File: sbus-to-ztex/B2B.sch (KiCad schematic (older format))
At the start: 8 parts, among them J1 Conn_01x06_Male, J3 Conn_02x07_Odd_Even

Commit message: Commit first go at v1.2
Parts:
- removed DOE2: RED, LED_SMD:LED_0805_2012Metric, symbol Device:LED_ALT
- removed ROE2: 549, Resistor_SMD:R_0603_1608Metric, symbol Device:R
- J1: footprint Connector_PinHeader_2.54mm:PinHeader_1x06_P2.54mm_Vertical -> Connector_PinHeader_2.54mm:PinHeader_1x06_P2.54mm_Horizontal; MPN 22-28-4060 -> 22-28-8060; MPN-ALT (none) -> PZ254R-11-06P; URL (none) -> https://www2.mouser.com/ProductDetail/Molex/22-28-8060?qs=4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
- J3: MPN 878331420 -> 87833-1420; MPN-ALT (none) -> A2005WR-N-2X7P-B; URL (none) -> https://www2.mouser.com/ProductDetail/Molex/87833-1420?qs=%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
- JAB1, JCD1: URL (none) -> https://www2.mouser.com/ProductDetail/Molex/10-89-7642?qs=%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
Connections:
- net SBUS_3V3_INT[4]*: now also JCD1.40 (N5~IO_L13P_T2_MRCC_34)
- net SBUS_3V3_INT[7]*: no longer JCD1.40 (N5~IO_L13P_T2_MRCC_34)
- net PMOD-8: now reaches JCD1.20 (U4~IO_L8P_T1_34)
- net LED0 renamed USBH0_D+
- net LED1 renamed USBH0_D-
- net LED2 renamed PMOD-12
- net LED3 renamed PMOD-11
- net LED4 renamed PMOD-10
- net LED5 renamed PMOD-9
- net LED6 renamed PMOD-7
- net LED7 renamed PMOD-5
- net SBUS_DATA_OE_LED_2 renamed PMOD-6
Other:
- note removed: "Free"
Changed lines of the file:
@@
 $Descr A4 11693 8268
 encoding utf-8
-Sheet 3 5
+Sheet 3 6
 Title "sbus-to-ztex B2B connector"
 Date ""
@@
 F 3 "" H 1800 2650 50  0001 C CNN
 F 4 "10-89-7642" H 1800 2650 50  0001 C CNN "MPN"
+F 5 "https://www2.mouser.com/ProductDetail/Molex/10-89-7642?qs=%2Fha2pyFadugCxzQFZUdvioDcljDVidgd4vXrOFuSRYM%3D" H 1800 2650 50  0001 C CNN "URL"
 	1    1800 2650
 	1    0    0    -1
@@
 Text GLabel 4100 2850 2    60   Input ~ 0
 SBUS_3V3_D[24]
-Text GLabel 9900 3050 2    60   Input ~ 0
+Text GLabel 6650 5700 2    60   Input ~ 0
 SBUS_3V3_INT[7]*
 Text GLabel 6300 5850 0    60   Input ~ 0
@@
 Text GLabel 6300 5950 0    60   Input ~ 0
 SBUS_3V3_INT[5]*
-Text GLabel 6300 6050 0    60   Input ~ 0
+Text GLabel 9900 3050 2    60   Input ~ 0
 SBUS_3V3_INT[4]*
 Text GLabel 6300 6150 0    60   Input ~ 0
@@
 Text GLabel 7400 2350 0    60   Input ~ 0
 SBUS_3V3_EER*
-Text GLabel 7400 1450 0    60   Input ~ 0
-LED0
-Text GLabel 7400 1550 0    60   Input ~ 0
-LED1
 Wire Wire Line
 	1800 5850 1650 5850
@@
 F 0 "J1" H 9356 1228 50  0000 C CNN
 F 1 "Conn_01x06_Male" H 9356 1137 50  0000 C CNN
-F 2 "Connector_PinHeader_2.54mm:PinHeader_1x06_P2.54mm_Vertical" H 9250 850 50  0001 C CNN
+F 2 "Connector_PinHeader_2.54mm:PinHeader_1x06_P2.54mm_Horizontal" H 9250 850 50  0001 C CNN
 F 3 "~" H 9250 850 50  0001 C CNN
-F 4 "22-28-4060" H 9250 850 50  0001 C CNN "MPN"
+F 4 "22-28-8060" H 9250 850 50  0001 C CNN "MPN"
+F 5 "PZ254R-11-06P" H 9250 850 50  0001 C CNN "MPN-ALT"
+F 6 "https://www2.mouser.com/ProductDetail/Molex/22-28-8060?qs=4XSMV6Twtb2rYD%2F%2F316gfQ==" H 9250 850 50  0001 C CNN "URL"
 	1    9250 850
 	1    0    0    -1
@@
 F 3 "" H 7600 2650 50  0001 C CNN
 F 4 "10-89-7642" H 7600 2650 50  0001 C CNN "MPN"
+F 5 "https://www2.mouser.com/ProductDetail/Molex/10-89-7642?qs=%2Fha2pyFadugCxzQFZUdvioDcljDVidgd4vXrOFuSRYM%3D" H 7600 2650 50  0001 C CNN "URL"
 	1    7600 2650
 	1    0    0    -1
 $EndComp
-Text GLabel 7400 1650 0    60   Input ~ 0
-LED2
-Text GLabel 7400 1750 0    60   Input ~ 0
-LED3
 Text GLabel 2800 5850 2    60   Input ~ 12
 SBUS_DATA_OE_LED
@@
 Text GLabel 9900 2350 2    60   Input ~ 12
 SBUS_DATA_OE_LED
-Wire Wire Line
-	1800 6400 1650 6400
-Wire Wire Line
-	1650 6400 1650 6600
-Wire Wire Line
-	2100 6400 2500 6400
-$Comp
-L Device:R ROE?
-U 1 1 5F75534A
-P 2650 6400
-AR Path="/5F6B165A/5F75534A" Ref="ROE?"  Part="1"
-AR Path="/5F67E4B9/5F75534A" Ref="ROE2"  Part="1"
-F 0 "ROE2" V 2730 6400 50  0000 C CNN
-F 1 "549" V 2650 6400 50  0000 C CNN
-F 2 "Resistor_SMD:R_0603_1608Metric" V 2580 6400 50  0001 C CNN
-F 3 "" H 2650 6400 50  0000 C CNN
-F 4 "0603WAF5490T5E" V 2650 6400 50  0001 C CNN "MPN"
-	1    2650 6400
-	0    1    1    0
-$EndComp
-Text Label 2150 6400 0    60   ~ 0
-DATA_OE_LED_2
-$Comp
-L Device:LED_ALT D?
-U 1 1 5F75535B
-P 1950 6400
-AR Path="/5F6B165A/5F75535B" Ref="D?"  Part="1"
-AR Path="/5F67E4B9/5F75535B" Ref="DOE2"  Part="1"
-F 0 "DOE2" H 1950 6500 50  0000 C CNN
-F 1 "RED" H 1600 6400 50  0000 R CNN
-F 2 "LED_SMD:LED_0805_2012Metric" H 1950 6400 50  0001 C CNN
-F 3 "https://optoelectronics.liteon.com/upload/download/DS-22-99-0150/LTST-C170KRKT.pdf" H 1950 6400 50  0001 C CNN
-F 4 "www.liteon.com" H 1950 6400 60  0001 C CNN "MNF1_URL"
-F 5 "LTST-C170KRKT" H 1950 6400 60  0001 C CNN "MPN"
-F 6 "859-LTST-C170KRKT" H 1950 6400 60  0001 C CNN "Mouser"
-F 7 "743-IN-S85ATR" H 1950 6400 50  0001 C CNN "Mouse_r2"
-F 8 "160-1415-1-ND" H 1950 6400 50  0001 C CNN "Digikey"
-F 9 "C94868" H 1950 6400 50  0001 C CNN "LCSC"
-F 10 "0.0195$" H 1950 6400 50  0001 C CNN "price400_LCSC"
-F 11 "FV007" H 1950 6400 50  0001 C CNN "Koncar"
-F 12 "TB" H 1950 6400 50  0001 C CNN "Side"
-	1    1950 6400
-	1    0    0    -1
-$EndComp
-$Comp
-L power:GND #PWR0120
-U 1 1 5F755362
-P 1650 6600
-F 0 "#PWR0120" H 1650 6350 50  0001 C CNN
-F 1 "GND" H 1655 6427 50  0000 C CNN
-F 2 "" H 1650 6600 50  0001 C CNN
-F 3 "" H 1650 6600 50  0001 C CNN
-	1    1650 6600
-	1    0    0    -1
-$EndComp
-Text GLabel 2800 6400 2    60   Input ~ 12
-SBUS_DATA_OE_LED_2
-Text GLabel 9900 2450 2    60   Input ~ 12
-SBUS_DATA_OE_LED_2
 $Comp
 L Connector_Generic:Conn_02x07_Odd_Even J3
@@
 F 2 "Connector_PinHeader_2.00mm:PinHeader_2x07_P2.00mm_Horizontal" H 3150 7250 50  0001 C CNN
 F 3 "https://www.molex.com/pdm_docs/sd/878331420_sd.pdf" H 3150 7250 50  0001 C CNN
-F 4 "878331420" H 3150 7250 50  0001 C CNN "MPN"
+F 4 "87833-1420" H 3150 7250 50  0001 C CNN "MPN"
+F 5 "A2005WR-N-2X7P-B" H 3150 7250 50  0001 C CNN "MPN-ALT"
+F 6 "https://www2.mouser.com/ProductDetail/Molex/87833-1420?qs=%2Fha2pyFadujYFYCIYI1IvFCvLi7no9WQYzIL%2FpYxKhg%3D" H 3150 7250 50  0001 C CNN "URL"
 	1    3150 7250
 	1    0    0    -1
@@
 Wire Wire Line
 	7150 1350 7400 1350
-Text GLabel 9900 3150 2    60   Input ~ 0
-LED4
-Text GLabel 9900 3250 2    60   Input ~ 0
-LED5
-Text GLabel 9900 3350 2    60   Input ~ 0
-LED6
-Text GLabel 9900 3450 2    60   Input ~ 0
-LED7
 Wire Wire Line
 	1450 2550 1600 2550
@@
 Wire Wire Line
 	9450 1050 10200 1050
-Text Notes 10100 2100 0    50   ~ 0
-Free
+Text GLabel 7400 1450 0    50   Input ~ 0
+USBH0_D+
+Text GLabel 7400 1550 0    50   Input ~ 0
+USBH0_D-
+Text GLabel 7400 1650 0    50   Input ~ 0
+PMOD-12
+Text GLabel 9900 3450 2    50   Input ~ 0
+PMOD-5
+Text GLabel 9900 2450 2    50   Input ~ 0
+PMOD-6
+Text GLabel 9900 3350 2    50   Input ~ 0
+PMOD-7
+Text GLabel 9900 2050 2    50   Input ~ 0
+PMOD-8
+Text GLabel 9900 3250 2    50   Input ~ 0
+PMOD-9
+Text GLabel 9900 3150 2    50   Input ~ 0
+PMOD-10
+Text GLabel 7400 1750 0    50   Input ~ 0
+PMOD-11
 $EndSCHEMATC

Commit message: fix footprints for SeeedStudio DRC results
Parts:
- J3: footprint Connector_PinHeader_2.00mm:PinHeader_2x07_P2.00mm_Horizontal -> For_SeeedStudio:PinHeader_2x07_P2.00mm_Horizontal_For_SeeedStudio
- JAB1, JCD1: footprint Connector_PinHeader_2.54mm:PinHeader_2x32_P2.54mm_Vertical -> For_SeeedStudio:PinHeader_2x32_P2.54mm_Vertical_For_SeeedStudio
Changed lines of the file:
@@
 F 0 "JAB1" H 1825 4375 50  0000 C CNN
 F 1 "ZTEX_AB-ztex_AB" H 1825 4284 50  0000 C CNN
-F 2 "Connector_PinHeader_2.54mm:PinHeader_2x32_P2.54mm_Vertical" H 1800 2650 50  0001 C CNN
+F 2 "For_SeeedStudio:PinHeader_2x32_P2.54mm_Vertical_For_SeeedStudio" H 1800 2650 50  0001 C CNN
 F 3 "" H 1800 2650 50  0001 C CNN
 F 4 "10-89-7642" H 1800 2650 50  0001 C CNN "MPN"
@@
 F 0 "JCD1" H 7650 4375 50  0000 C CNN
 F 1 "ZTEX_CD-ztex_CD" H 7650 4284 50  0000 C CNN
-F 2 "Connector_PinHeader_2.54mm:PinHeader_2x32_P2.54mm_Vertical" H 7600 2650 50  0001 C CNN
+F 2 "For_SeeedStudio:PinHeader_2x32_P2.54mm_Vertical_For_SeeedStudio" H 7600 2650 50  0001 C CNN
 F 3 "" H 7600 2650 50  0001 C CNN
 F 4 "10-89-7642" H 7600 2650 50  0001 C CNN "MPN"
@@
 F 0 "J3" H 3200 7767 50  0000 C CNN
 F 1 "Conn_02x07_Odd_Even" H 3200 7676 50  0000 C CNN
-F 2 "Connector_PinHeader_2.00mm:PinHeader_2x07_P2.00mm_Horizontal" H 3150 7250 50  0001 C CNN
+F 2 "For_SeeedStudio:PinHeader_2x07_P2.00mm_Horizontal_For_SeeedStudio" H 3150 7250 50  0001 C CNN
 F 3 "https://www.molex.com/pdm_docs/sd/878331420_sd.pdf" H 3150 7250 50  0001 C CNN
 F 4 "87833-1420" H 3150 7250 50  0001 C CNN "MPN"

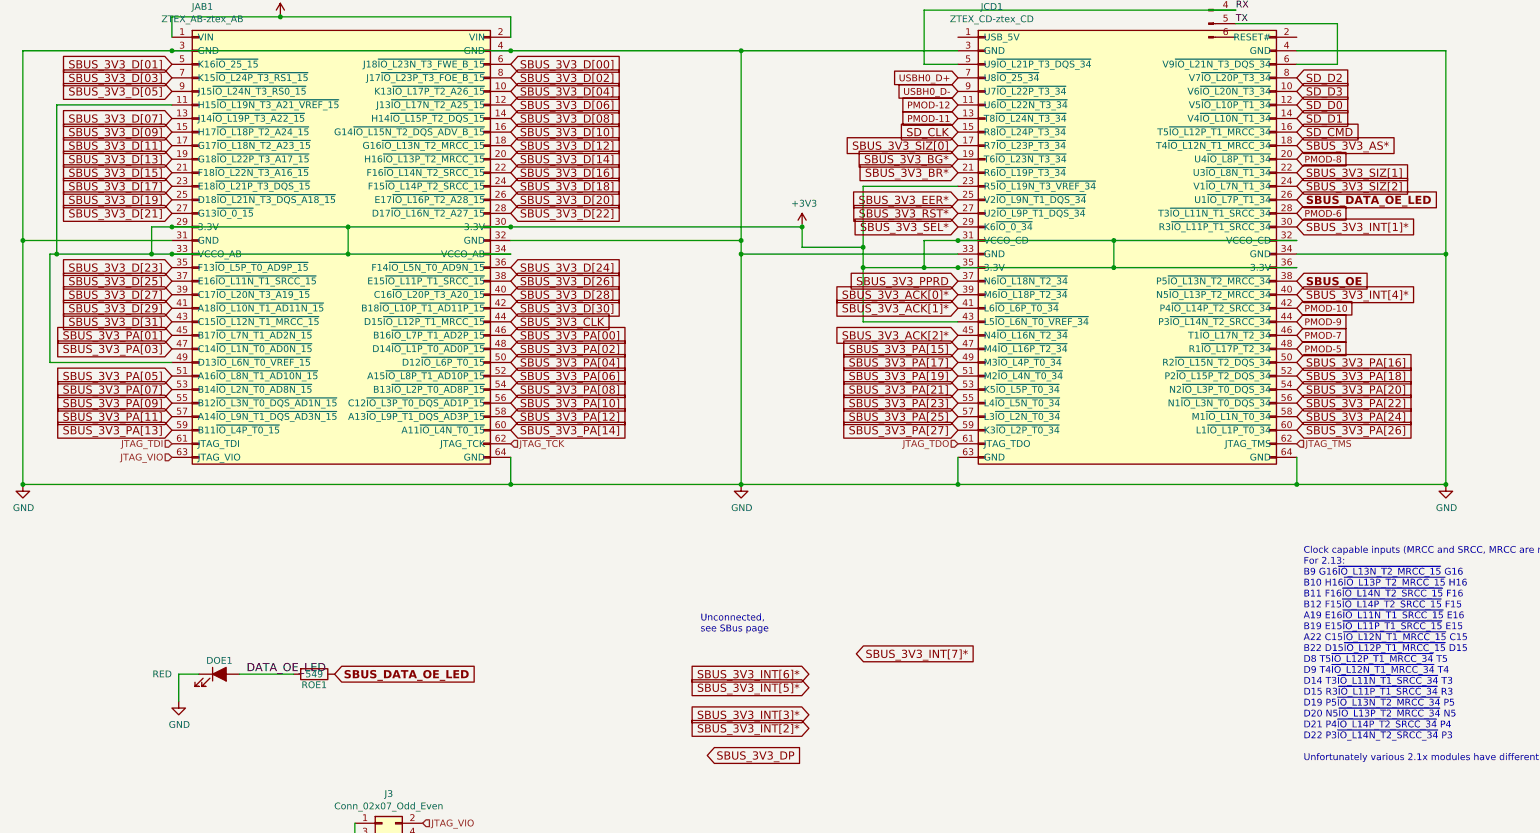
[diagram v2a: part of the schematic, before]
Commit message: update some MPN w/ SeeedStudio replacement
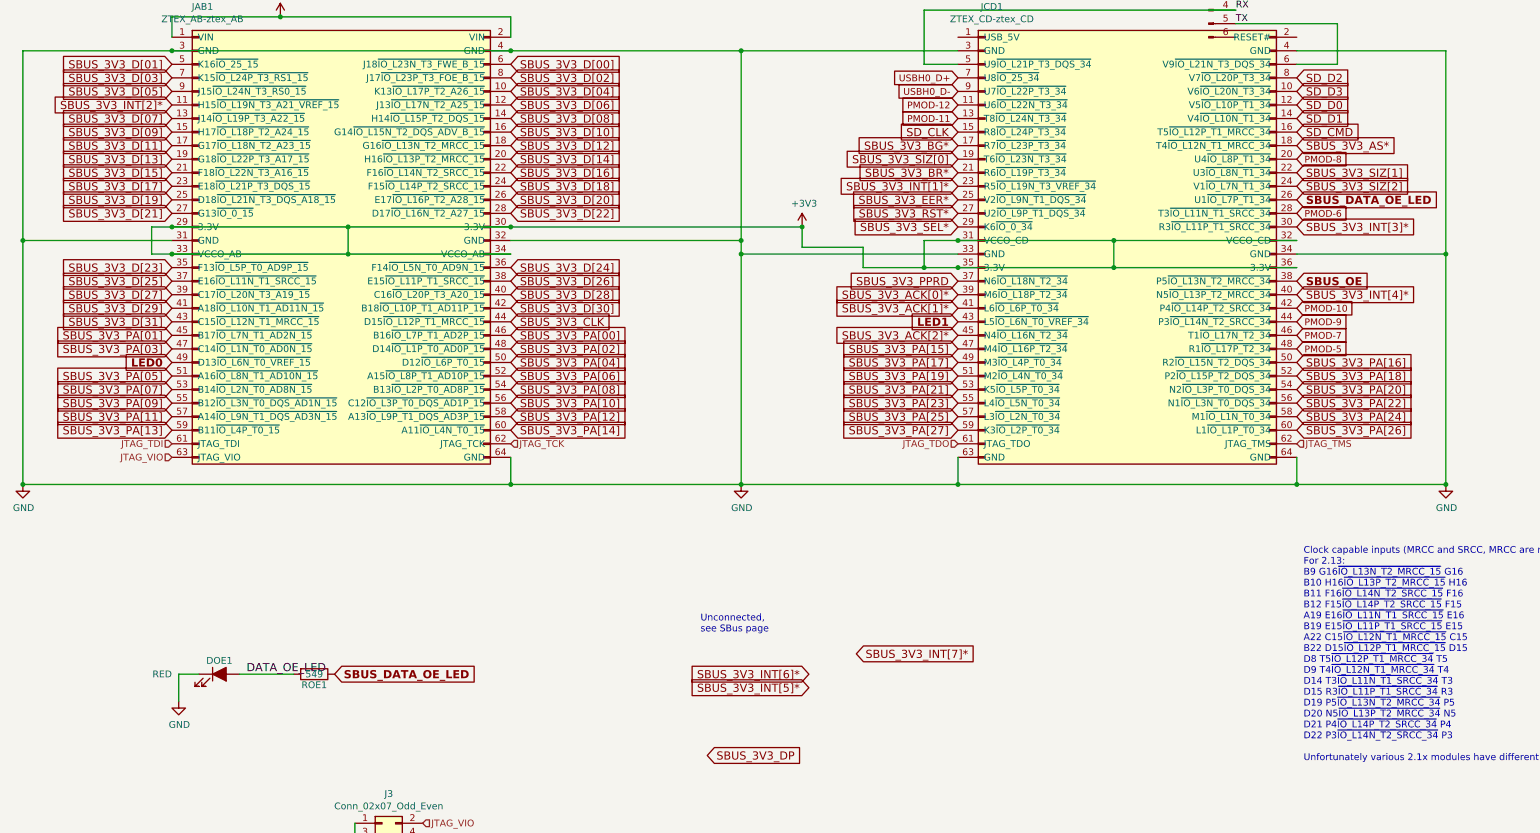
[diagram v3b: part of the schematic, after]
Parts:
- J1: footprint Connector_PinHeader_2.54mm:PinHeader_1x06_P2.54mm_Horizontal -> For_SeeedStudio:PinHeader_1x06_P2.54mm_Horizontal_For_SeeedStudio; MPN 22-28-8060 -> PZ254R-11-06P; MPN-ALT PZ254R-11-06P -> 22-28-8060; URL https://www2.mouser.com/ProductDetail/Molex/22-28-8060?qs=4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 -> (none); URL-ALT (none) -> https://www2.mouser.com/ProductDetail/Molex/22-28-8060?qs=4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
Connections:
- net +3V3: no longer JAB1.11 (H15~IO_L19N_T3_A21_VREF_15), JAB1.49 (D13~IO_L6N_T0_VREF_15), JCD1.23 (R5~IO_L19N_T3_VREF_34), JCD1.43 (L5~IO_L6N_T0_VREF_34)
- net SBUS_3V3_BG*: now also JCD1.17 (R7~IO_L23P_T3_34); no longer JCD1.19 (T6~IO_L23N_T3_34)
- net SBUS_3V3_INT[1]*: now also JCD1.23 (R5~IO_L19N_T3_VREF_34); no longer JCD1.30 (R3~IO_L11P_T1_SRCC_34)
- net SBUS_3V3_INT[2]*: now also JAB1.11 (H15~IO_L19N_T3_A21_VREF_15)
- net SBUS_3V3_INT[3]*: now also JCD1.30 (R3~IO_L11P_T1_SRCC_34)
- net SBUS_3V3_SIZ[0]: now also JCD1.19 (T6~IO_L23N_T3_34); no longer JCD1.17 (R7~IO_L23P_T3_34)
- new net LED0: JAB1.49 (D13~IO_L6N_T0_VREF_15)
- new net LED1: JCD1.43 (L5~IO_L6N_T0_VREF_34)
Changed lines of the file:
@@
 Text GLabel 4100 1850 2    60   Input ~ 0
 SBUS_3V3_D[10]
-Wire Wire Line
-	1600 1650 750  1650
-Wire Wire Line
-	750  1650 750  2750
-Wire Wire Line
-	750  2750 1450 2750
-Connection ~ 1450 2750
-Wire Wire Line
-	7400 2250 6700 2250
-Wire Wire Line
-	6700 2250 6700 2700
-Connection ~ 6700 2850
-Wire Wire Line
-	7400 3250 6700 3250
-Wire Wire Line
-	6700 3250 6700 2850
-Wire Wire Line
-	1600 3550 700  3550
-Wire Wire Line
-	700  3550 700  2750
-Wire Wire Line
-	700  2750 750  2750
-Connection ~ 750  2750
 Text GLabel 4100 2150 2    60   Input ~ 0
 SBUS_3V3_D[16]
@@
 Text GLabel 9900 3050 2    60   Input ~ 0
 SBUS_3V3_INT[4]*
-Text GLabel 6300 6150 0    60   Input ~ 0
+Text GLabel 9900 2550 2    60   Input ~ 0
 SBUS_3V3_INT[3]*
-Text GLabel 6300 6250 0    60   Input ~ 0
+Text GLabel 1600 1650 0    60   Input ~ 0
 SBUS_3V3_INT[2]*
-Text GLabel 9900 2550 2    60   Input ~ 0
+Text GLabel 7400 2250 0    60   Input ~ 0
 SBUS_3V3_INT[1]*
 Text GLabel 4100 3350 2    60   Input ~ 0
@@
 Text GLabel 5550 6450 2    60   Input ~ 0
 SBUS_3V3_DP
-Text GLabel 7400 1950 0    60   Input ~ 0
+Text GLabel 7400 2050 0    60   Input ~ 0
 SBUS_3V3_SIZ[0]
 Text GLabel 9900 2150 2    60   Input ~ 0
@@
 Text GLabel 7400 2550 0    60   Input ~ 0
 SBUS_3V3_SEL*
-Text GLabel 7400 2050 0    60   Input ~ 0
+Text GLabel 7400 1950 0    60   Input ~ 0
 SBUS_3V3_BG*
 Text GLabel 9900 1950 2    60   Input ~ 0
@@
 F 0 "J1" H 9356 1228 50  0000 C CNN
 F 1 "Conn_01x06_Male" H 9356 1137 50  0000 C CNN
-F 2 "Connector_PinHeader_2.54mm:PinHeader_1x06_P2.54mm_Horizontal" H 9250 850 50  0001 C CNN
+F 2 "For_SeeedStudio:PinHeader_1x06_P2.54mm_Horizontal_For_SeeedStudio" H 9250 850 50  0001 C CNN
 F 3 "~" H 9250 850 50  0001 C CNN
-F 4 "22-28-8060" H 9250 850 50  0001 C CNN "MPN"
-F 5 "PZ254R-11-06P" H 9250 850 50  0001 C CNN "MPN-ALT"
-F 6 "https://www2.mouser.com/ProductDetail/Molex/22-28-8060?qs=4XSMV6Twtb2rYD%2F%2F316gfQ==" H 9250 850 50  0001 C CNN "URL"
+F 4 "22-28-8060" H 9250 850 50  0001 C CNN "MPN-ALT"
+F 5 "PZ254R-11-06P" H 9250 850 50  0001 C CNN "MPN"
+F 6 "https://www2.mouser.com/ProductDetail/Molex/22-28-8060?qs=4XSMV6Twtb2rYD%2F%2F316gfQ==" H 9250 850 50  0001 C CNN "URL-ALT"
 	1    9250 850
 	1    0    0    -1
@@
 	6250 2700 6700 2700
 Connection ~ 4100 2550
-Connection ~ 6700 2700
 Wire Wire Line
 	6700 2700 6700 2850
@@
 Text GLabel 7400 1750 0    50   Input ~ 0
 PMOD-11
+Text GLabel 1600 3550 0    60   Input ~ 12
+LED0
+Text GLabel 7400 3250 0    60   Input ~ 12
+LED1
 $EndSCHEMATC

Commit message: more up-to-date
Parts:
- J1: URL (none) -> https://lcsc.com/product-detail/Pin-Header-Female-Header_XF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
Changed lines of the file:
@@
 F 5 "PZ254R-11-06P" H 9250 850 50  0001 C CNN "MPN"
 F 6 "https://www2.mouser.com/ProductDetail/Molex/22-28-8060?qs=4XSMV6Twtb2rYD%2F%2F316gfQ==" H 9250 850 50  0001 C CNN "URL-ALT"
+F 7 "https://lcsc.com/product-detail/Pin-Header-Female-Header_XFCN-PZ254R-11-06P_C492414.html" H 9250 850 50  0001 C CNN "URL"
 	1    9250 850
 	1    0    0    -1
